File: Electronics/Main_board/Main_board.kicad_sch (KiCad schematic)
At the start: 1 part

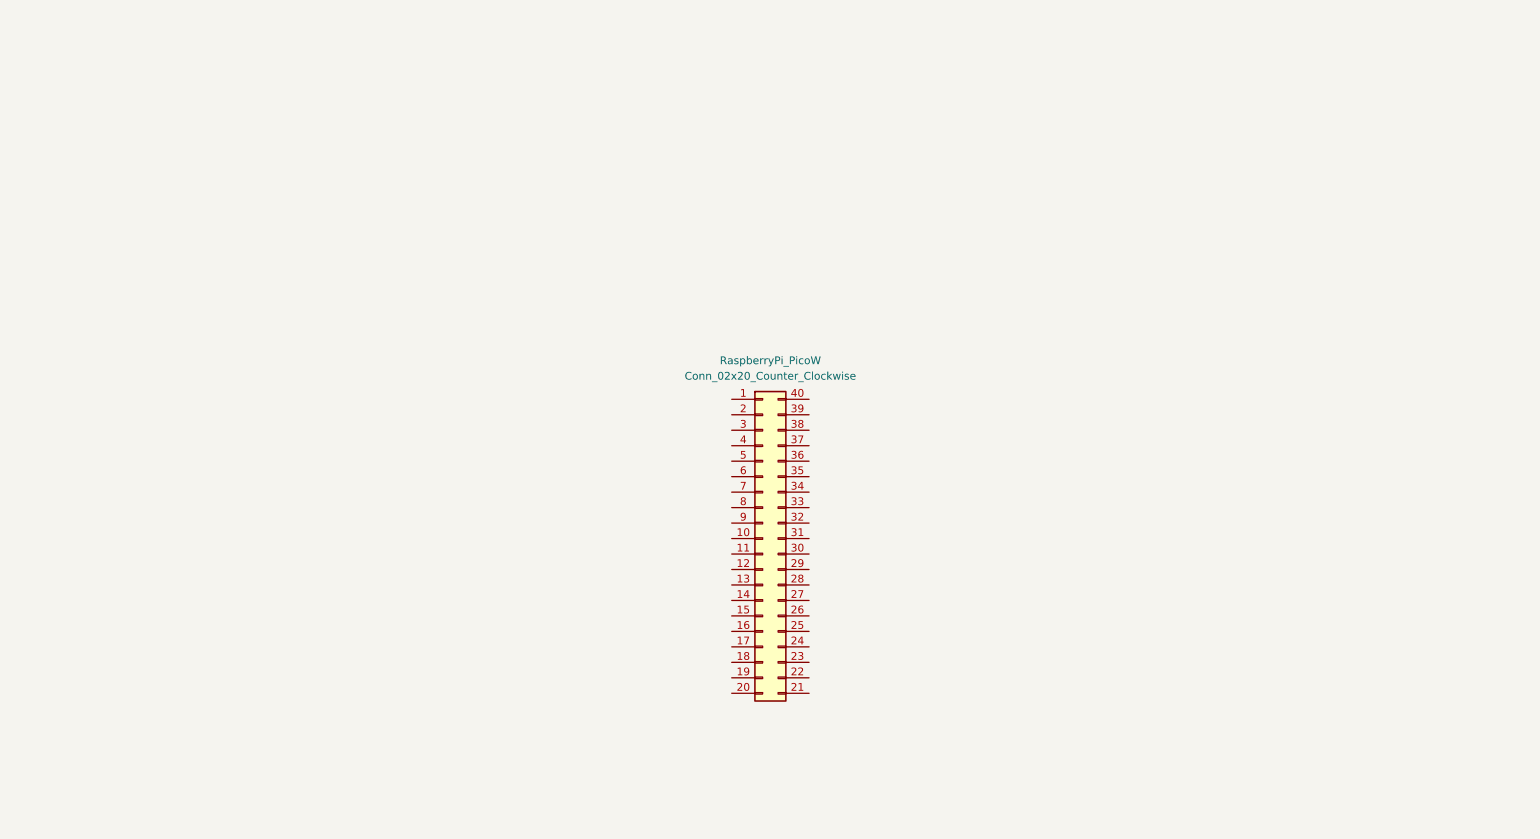
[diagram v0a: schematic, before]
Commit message: Main MCU now communicate with multiple nRF. Added Main Board Schematic
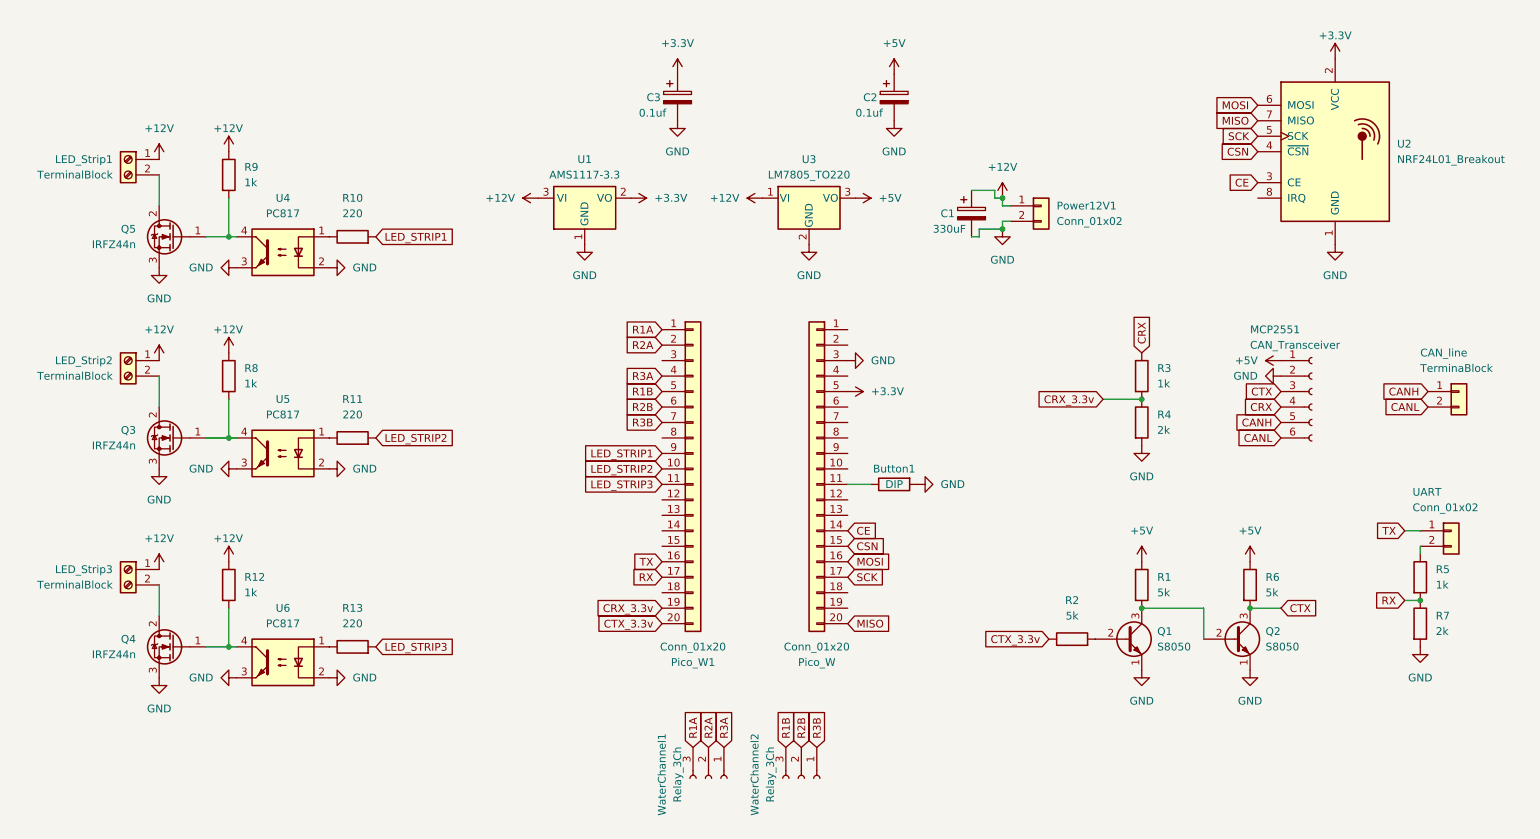
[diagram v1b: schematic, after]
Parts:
- removed RaspberryPi_PicoW: Conn_02x20_Counter_Clockwise, symbol Connector_Generic:Conn_02x20_Counter_Clockwise
- added Button1: DIP, Resistor_THT:R_Axial_DIN0207_L6.3mm_D2.5mm_P5.08mm_Vertical, symbol Device:R
- added C1: 330uF, Capacitor_THT:CP_Radial_D8.0mm_P3.80mm, symbol Device:C_Polarized
- added C2, C3: 0.1uf, Capacitor_THT:CP_Radial_D4.0mm_P2.00mm, symbol Device:C_Polarized
- added CAN_line: TerminaBlock, TerminalBlock:TerminalBlock_bornier-2_P5.08mm, symbol Connector_Generic:Conn_01x02
- added LED_Strip1, LED_Strip2, LED_Strip3: TerminalBlock, TerminalBlock:TerminalBlock_bornier-2_P5.08mm, symbol Connector:Screw_Terminal_01x02
- added MCP2551: CAN_Transceiver, Connector_PinSocket_2.54mm:PinSocket_1x06_P2.54mm_Vertical, symbol Connector:Conn_01x06_Socket
- added Pico_W, Pico_W1: Conn_01x20, Connector_PinSocket_2.54mm:PinSocket_1x20_P2.54mm_Vertical, symbol Connector_Generic:Conn_01x20
- added Power12V1, UART: Conn_01x02, Connector_JST:JST_EH_B2B-EH-A_1x02_P2.50mm_Vertical, symbol Connector_Generic:Conn_01x02
- added Q1, Q2: S8050, Package_TO_SOT_THT:TO-92_Inline_Wide, symbol Transistor_BJT:S8050
- added Q3, Q4, Q5: IRFZ44n, Package_TO_SOT_THT:TO-220-3_Vertical, symbol Transistor_FET:IRF540N
- added R1, R2, R6: 5k, Resistor_THT:R_Axial_DIN0207_L6.3mm_D2.5mm_P7.62mm_Horizontal, symbol Device:R
- added R10, R11, R13: 220, Resistor_THT:R_Axial_DIN0207_L6.3mm_D2.5mm_P7.62mm_Horizontal, symbol Device:R
- added R12, R3, R5, R8, R9: 1k, Resistor_THT:R_Axial_DIN0207_L6.3mm_D2.5mm_P7.62mm_Horizontal, symbol Device:R
- added R4, R7: 2k, Resistor_THT:R_Axial_DIN0207_L6.3mm_D2.5mm_P7.62mm_Horizontal, symbol Device:R
- added U1: AMS1117-3.3, Package_TO_SOT_THT:TO-220-3_Vertical, symbol Regulator_Linear:AMS1117-3.3
- added U2: NRF24L01_Breakout, RF_Module:nRF24L01_Breakout, symbol RF:NRF24L01_Breakout
- added U3: LM7805_TO220, Package_TO_SOT_THT:TO-220-3_Vertical, symbol Regulator_Linear:LM7805_TO220
- added U4, U5, U6: PC817, Package_DIP:DIP-4_W7.62mm, symbol Isolator:PC817
- added WaterChannel1, WaterChannel2: Relay_3Ch, Connector_JST:JST_EH_B3B-EH-A_1x03_P2.50mm_Vertical, symbol Connector:Conn_01x03_Socket
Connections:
- new net: R13.1, U6.1
- new net: R10.1, U4.1
- new net: Q5.1 (G), R9.2, U4.4
- new net: R11.1, U5.1
- new net: Q3.1 (G), R8.2, U5.4
- new net: Q1.2 (B), R2.2
- new net: Q1.3 (C), Q2.2 (B), R1.2
- new net: Button1.1, Pico_W.11 (Pin_11)
- new net: R5.1, UART.2 (Pin_2)
- new net: Q4.1 (G), R12.2, U6.4
- new net: LED_Strip3.2 (Pin_2), Q4.2 (D)
- new net: LED_Strip2.2 (Pin_2), Q3.2 (D)
- new net: LED_Strip1.2 (Pin_2), Q5.2 (D)
- new net +12V: C1.1, LED_Strip1.1 (Pin_1), LED_Strip2.1 (Pin_1), LED_Strip3.1 (Pin_1), Power12V1.1 (Pin_1), R12.1, R8.1, R9.1, U1.3 (VI), U3.1 (VI)
- new net +3.3V: C3.1, Pico_W.5 (Pin_5), U1.2 (VO), U2.2 (VCC)
- new net +5V: C2.1, MCP2551.1 (Pin_1), R1.1, R6.1, U3.3 (VO)
- new net CANH: CAN_line.1 (Pin_1), MCP2551.5 (Pin_5)
- new net CANL: CAN_line.2 (Pin_2), MCP2551.6 (Pin_6)
- new net CE: Pico_W.14 (Pin_14), U2.3 (CE)
- new net CRX: MCP2551.4 (Pin_4), R3.1
- new net CRX_3.3v: Pico_W1.19 (Pin_19), R3.2, R4.1
- new net CSN: Pico_W.15 (Pin_15), U2.4 (~{CSN})
- new net CTX: MCP2551.3 (Pin_3), Q2.3 (C), R6.2
- new net CTX_3.3v: Pico_W1.20 (Pin_20), R2.1
- new net GND: Button1.2, C1.2, C2.2, C3.2, MCP2551.2 (Pin_2), Pico_W.3 (Pin_3), Power12V1.2 (Pin_2), Q1.1 (E), Q2.1 (E), Q3.3 (S), Q4.3 (S), Q5.3 (S), R4.2, R7.2, U1.1 (GND), U2.1 (GND), U3.2 (GND), U4.2, U4.3, U5.2, U5.3, U6.2, U6.3
- new net LED_STRIP1: Pico_W1.9 (Pin_9), R10.2
- new net LED_STRIP2: Pico_W1.10 (Pin_10), R11.2
- new net LED_STRIP3: Pico_W1.11 (Pin_11), R13.2
- new net MISO: Pico_W.20 (Pin_20), U2.7 (MISO)
- new net MOSI: Pico_W.16 (Pin_16), U2.6 (MOSI)
- new net R1A: Pico_W1.1 (Pin_1), WaterChannel1.3 (Pin_3)
- new net R1B: Pico_W1.5 (Pin_5), WaterChannel2.3 (Pin_3)
- new net R2A: Pico_W1.2 (Pin_2), WaterChannel1.2 (Pin_2)
- new net R2B: Pico_W1.6 (Pin_6), WaterChannel2.2 (Pin_2)
- new net R3A: Pico_W1.4 (Pin_4), WaterChannel1.1 (Pin_1)
- new net R3B: Pico_W1.7 (Pin_7), WaterChannel2.1 (Pin_1)
- new net RX: Pico_W1.17 (Pin_17), R5.2, R7.1
- new net SCK: Pico_W.17 (Pin_17), U2.5 (SCK)
- new net TX: Pico_W1.16 (Pin_16), UART.1 (Pin_1)

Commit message: Main Board Code re-written; finished actuators, html pages and started server-side handling
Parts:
- renumbered CAN_line to CAN_line1, Pico_W to Pico_W2, UART to UART1
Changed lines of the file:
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@@
   (symbol (lib_id "Connector_Generic:Conn_01x02") (at 264.16 83.82 0) (unit 1)
     (in_bom yes) (on_board yes) (dnp no)
-    (property "Reference" "CAN_line" (at 257.81 77.47 0)
+    (property "Reference" "CAN_line1" (at 257.81 77.47 0)
       (effects (font (size 1.27 1.27)) (justify left))
     )
@@
       (project "Main_board"
         (path "/7d596dee-6f09-4134-b16f-bd56a6d790ef"
-          (reference "CAN_line") (unit 1)
+          (reference "CAN_line1") (unit 1)
         )
       )
@@
   (symbol (lib_id "Connector_Generic:Conn_01x20") (at 158.75 96.52 0) (mirror y) (unit 1)
     (in_bom yes) (on_board yes) (dnp no)
-    (property "Reference" "Pico_W" (at 158.75 128.27 0)
+    (property "Reference" "Pico_W2" (at 158.75 128.27 0)
       (effects (font (size 1.27 1.27)))
     )
@@
       (project "Main_board"
         (path "/7d596dee-6f09-4134-b16f-bd56a6d790ef"
-          (reference "Pico_W") (unit 1)
+          (reference "Pico_W2") (unit 1)
         )
       )
@@
   (symbol (lib_id "Connector_Generic:Conn_01x02") (at 262.89 106.68 0) (unit 1)
     (in_bom yes) (on_board yes) (dnp no)
-    (property "Reference" "UART" (at 256.54 100.33 0)
+    (property "Reference" "UART1" (at 256.54 100.33 0)
       (effects (font (size 1.27 1.27)) (justify left))
     )
@@
       (project "Main_board"
         (path "/7d596dee-6f09-4134-b16f-bd56a6d790ef"
-          (reference "UART") (unit 1)
-        )
-      )
+          (reference "UART1") (unit 1)
+        )
+      )

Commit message: finished Main Board PCB
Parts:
- added H1, H2: MountingHole, MountingHole:MountingHole_3.2mm_M3_DIN965_Pad_TopBottom, symbol Mechanical:MountingHole
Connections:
- net CRX_3.3v: now also Pico_W2.9 (Pin_9); no longer Pico_W1.19 (Pin_19)
- net CTX_3.3v: now also Pico_W2.10 (Pin_10); no longer Pico_W1.20 (Pin_20)
- net GND: now also Pico_W2.13 (Pin_13)
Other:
- moved on the sheet: LED_Strip1, LED_Strip2, LED_Strip3, Q3, Q4, Q5, R10, R11, R12, R13, R8, R9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
